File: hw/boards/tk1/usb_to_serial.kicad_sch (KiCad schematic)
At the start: 10 parts

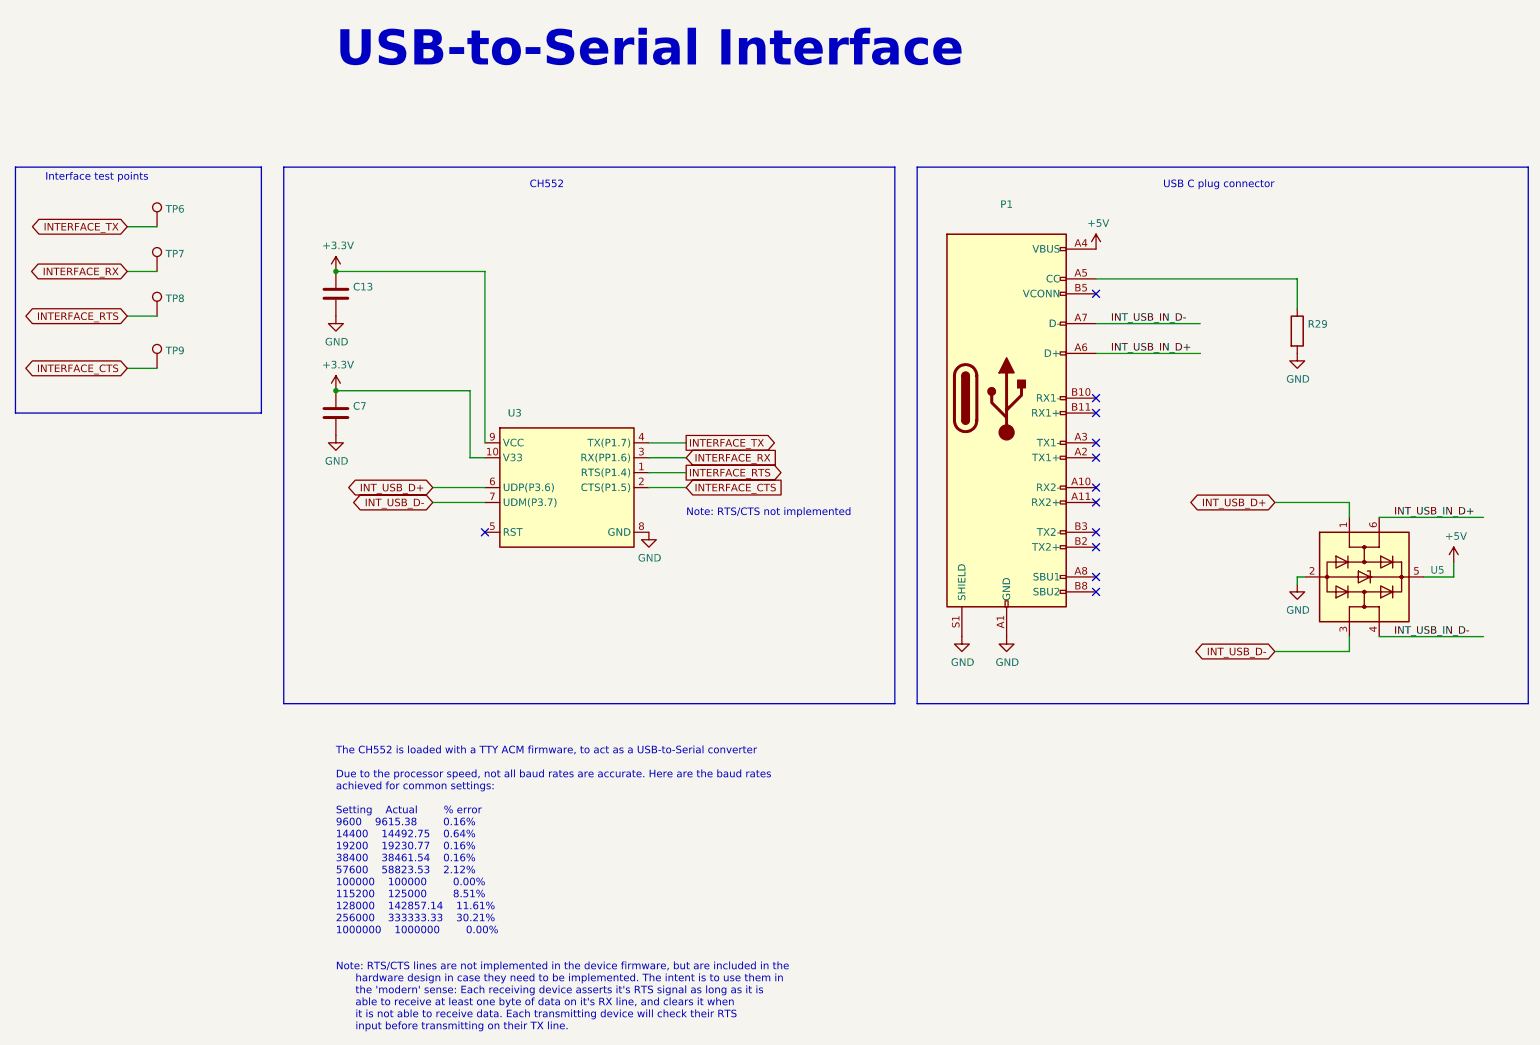
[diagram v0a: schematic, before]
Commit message: TK-1 and TP-1 PCBs (#52)
* Add kicad library for flat programming clip

* Add descriptions to part symbols

* Add extended values, manufacturer/distributor info to components in mta1

* Add new board entry for TK1

* Add TP1 programmer design

* Update MTA1-USB-V1 release files to match production

* Change SPI flash memory type to XT25F08BDFIGT-S
* Change touch sensor feedback cap to 1uF
* Add manufacturer, manufacturer part number, distributor, distributor part number

* Update component values for TK1 PCB

* Use specific part # for C8
* Change flash back to Winbond part, for easier sourcing
* Change C1 to 1pF

* Fixes for production programmer PCB

* Swap GND and 5V on J3
* Replace graphic logo with text
* Rename part to 'TP-1'

* TK-1 release

* Add dimensions for PCB
* Add layer stackup for PCB
* Change PCB component origin to match expanded board
* Change schematic title to 'TK-1', update release date

* mta1-usb-v1-programmer: Add corrected part numbers for OSFC production

* Q1, Q2, F1 part subsititutions
* add mfr/supplier info for all parts

* PCB library: add parts

* Rectangular footprint for TK-1 test pads
* BOM generation script used for TK-1 and TP-1 releases

* TP-1 release

* Schematic: Add manufacturer, supplier information for all parts
* Schematic: Update name and release date
* PCB: Add PCB fabrication information
* PCB: Correct pinouts on silkscreen

* PCB library: add 'screw' and 'foot' symbols

* Screw is a schematic-only part, for including mechanical screws in the
  BOM
* Foot is for self-adhesive rubber mounting feet that can be stuck to
  the bottom of a PCB

* TP-1 release: Add screws, feet to the BOM

* Pico library: Add footprint for RPi Pico w/solder paste

* TP-1 RevA release updates:

* Add fiducials in 3 corners (1mm exposed copper ring w/2mm soldermask opening)
* Add solder paste openings to Raspberry Pi Pico pads

* TK-1: RevA.1 release

* Add two fiducials to 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
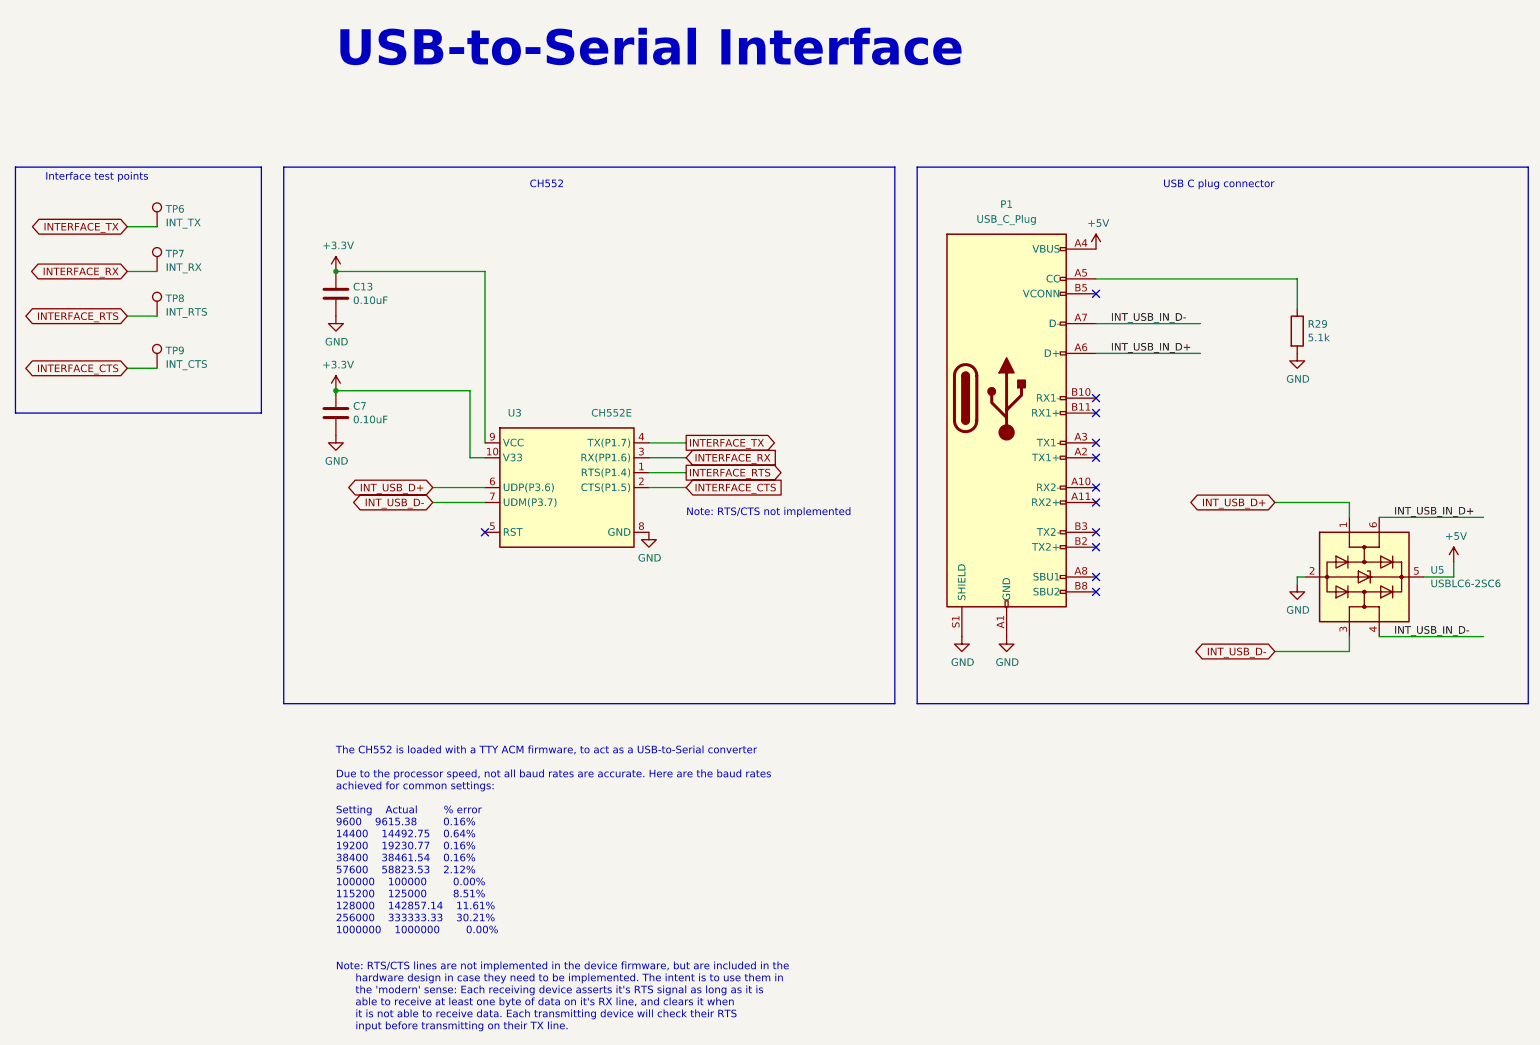
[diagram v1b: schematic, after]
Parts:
- C13, C7: value (none) -> 0.10uF; footprint (none) -> mta1:CAPC1005X06L
- P1: value (none) -> USB_C_Plug; footprint (none) -> mta1:U261-241N-4BS60
- R29: value (none) -> 5.1k; footprint (none) -> mta1:ERJ2G(0402)_L
- TP6: value (none) -> INT_TX; footprint (none) -> mta1:TestPoint_Pad_D1.0mm
- TP7: value (none) -> INT_RX; footprint (none) -> mta1:TestPoint_Pad_D1.0mm
- TP8: value (none) -> INT_RTS; footprint (none) -> mta1:TestPoint_Pad_D1.0mm
- TP9: value (none) -> INT_CTS; footprint (none) -> mta1:TestPoint_Pad_D1.0mm
- U3: value (none) -> CH552E; footprint (none) -> Package_SO:MSOP-10_3x3mm_P0.5mm
- U5: value (none) -> USBLC6-2SC6; footprint (none) -> Package_TO_SOT_SMD:SOT-23-6
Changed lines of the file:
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@@
   (title_block
     (title "USB-to-Serial Interface")
-    (date "2021-09-29")
+    (date "2021-11-14")
     (rev "V1")
     (company "Tillitis AB")
@@
       (effects (font (size 1.27 1.27)) (justify left))
     )
-    (property "Value" "" (id 1) (at 262.7376 114.173 90)
-      (effects (font (size 1.27 1.27)) (justify left))
-    )
-    (property "Footprint" "" (id 2) (at 238.76 113.03 0)
+    (property "Value" "USBLC6-2SC6" (id 1) (at 262.7376 114.173 90)
+      (effects (font (size 1.27 1.27)) (justify left))
+    )
+    (property "Footprint" "Package_TO_SOT_SMD:SOT-23-6" (id 2) (at 238.76 113.03 0)
       (effects (font (size 1.27 1.27)) hide)
     )
@@
       (effects (font (size 1.27 1.27)) (justify left))
     )
-    (property "Value" "" (id 1) (at 79.121 65.913 0)
-      (effects (font (size 1.27 1.27)) (justify left))
-    )
-    (property "Footprint" "" (id 2) (at 77.1652 68.58 0)
+    (property "Value" "0.10uF" (id 1) (at 79.121 65.913 0)
+      (effects (font (size 1.27 1.27)) (justify left))
+    )
+    (property "Footprint" "mta1:CAPC1005X06L" (id 2) (at 77.1652 68.58 0)
       (effects (font (size 1.27 1.27)) hide)
     )
@@
       (effects (font (size 1.27 1.27)) (justify left))
     )
-    (property "Value" "" (id 1) (at 47.1932 60.2742 0)
-      (effects (font (size 1.27 1.27)) (justify left))
-    )
-    (property "Footprint" "" (id 2) (at 50.8 60.96 0)
+    (property "Value" "INT_RX" (id 1) (at 47.1932 60.2742 0)
+      (effects (font (size 1.27 1.27)) (justify left))
+    )
+    (property "Footprint" "mta1:TestPoint_Pad_D1.0mm" (id 2) (at 50.8 60.96 0)
       (effects (font (size 1.27 1.27)) hide)
     )
@@
       (effects (font (size 1.27 1.27)) (justify left))
     )
-    (property "Value" "" (id 1) (at 47.1932 67.8942 0)
-      (effects (font (size 1.27 1.27)) (justify left))
-    )
-    (property "Footprint" "" (id 2) (at 50.8 68.58 0)
+    (property "Value" "INT_RTS" (id 1) (at 47.1932 67.8942 0)
+      (effects (font (size 1.27 1.27)) (justify left))
+    )
+    (property "Footprint" "mta1:TestPoint_Pad_D1.0mm" (id 2) (at 50.8 68.58 0)
       (effects (font (size 1.27 1.27)) hide)
     )
@@
       (effects (font (size 1.27 1.27)) (justify left))
     )
-    (property "Value" "" (id 1) (at 79.121 86.233 0)
-      (effects (font (size 1.27 1.27)) (justify left))
-    )
-    (property "Footprint" "" (id 2) (at 77.1652 88.9 0)
+    (property "Value" "0.10uF" (id 1) (at 79.121 86.233 0)
+      (effects (font (size 1.27 1.27)) (justify left))
+    )
+    (property "Footprint" "mta1:CAPC1005X06L" (id 2) (at 77.1652 88.9 0)
       (effects (font (size 1.27 1.27)) hide)
     )
@@
     (in_bom yes) (on_board yes) (fields_autoplaced)
     (property "Reference" "P1" (id 0) (at 190.5 49.53 0))
-    (property "Value" "" (id 1) (at 190.5 52.07 0))
-    (property "Footprint" "" (id 2) (at 194.31 82.55 0)
+    (property "Value" "USB_C_Plug" (id 1) (at 190.5 52.07 0))
+    (property "Footprint" "mta1:U261-241N-4BS60" (id 2) (at 194.31 82.55 0)
       (effects (font (size 1.27 1.27)) hide)
     )
@@
       (effects (font (size 1.27 1.27)) (justify left))
     )
-    (property "Value" "" (id 1) (at 241.808 72.263 0)
-      (effects (font (size 1.27 1.27)) (justify left))
-    )
-    (property "Footprint" "" (id 2) (at 238.252 71.12 90)
+    (property "Value" "5.1k" (id 1) (at 241.808 72.263 0)
+      (effects (font (size 1.27 1.27)) (justify left))
+    )
+    (property "Footprint" "mta1:ERJ2G(0402)_L" (id 2) (at 238.252 71.12 90)
       (effects (font (size 1.27 1.27)) hide)
     )
@@
     (in_bom yes) (on_board yes)
     (property "Reference" "U3" (id 0) (at 106.68 85.09 0))
-    (property "Value" "" (id 1) (at 123.19 85.09 0))
-    (property "Footprint" "" (id 2) (at 172.72 107.95 0)
+    (property "Value" "CH552E" (id 1) (at 123.19 85.09 0))
+    (property "Footprint" "Package_SO:MSOP-10_3x3mm_P0.5mm" (id 2) (at 172.72 107.95 0)
       (effects (font (size 1.27 1.27)) hide)
     )
@@
       (effects (font (size 1.27 1.27)) (justify left))
     )
-    (property "Value" "" (id 1) (at 47.1932 76.7842 0)
-      (effects (font (size 1.27 1.27)) (justify left))
-    )
-    (property "Footprint" "" (id 2) (at 50.8 77.47 0)
+    (property "Value" "INT_CTS" (id 1) (at 47.1932 76.7842 0)
+      (effects (font (size 1.27 1.27)) (justify left))
+    )
+    (property "Footprint" "mta1:TestPoint_Pad_D1.0mm" (id 2) (at 50.8 77.47 0)
       (effects (font (size 1.27 1.27)) hide)
     )
@@
       (effects (font (size 1.27 1.27)) (justify left))
     )
-    (property "Value" "" (id 1) (at 47.1932 52.6542 0)
-      (effects (font (size 1.27 1.27)) (justify left))
-    )
-    (property "Footprint" "" (id 2) (at 50.8 53.34 0)
-      (effects (font (size 1.27 1.27)) hide)
-    )
+    (property "Value" "INT_TX" (id 1) (at 47.1932 52.6542 0)
+      (effects (font (size 1.27 1.27)) (justify left))
+    )
+    (property "Footprint" "mta1:TestPoint_Pad_D1.0mm" (id 2) (at 50.8 53.34 0)
+      (effects (font (size 1.27 1.27)) hide)
+    )
